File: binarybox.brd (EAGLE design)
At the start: 148.6 x 81.6 mm, 39 parts, among them IC2 MAX7219CNG

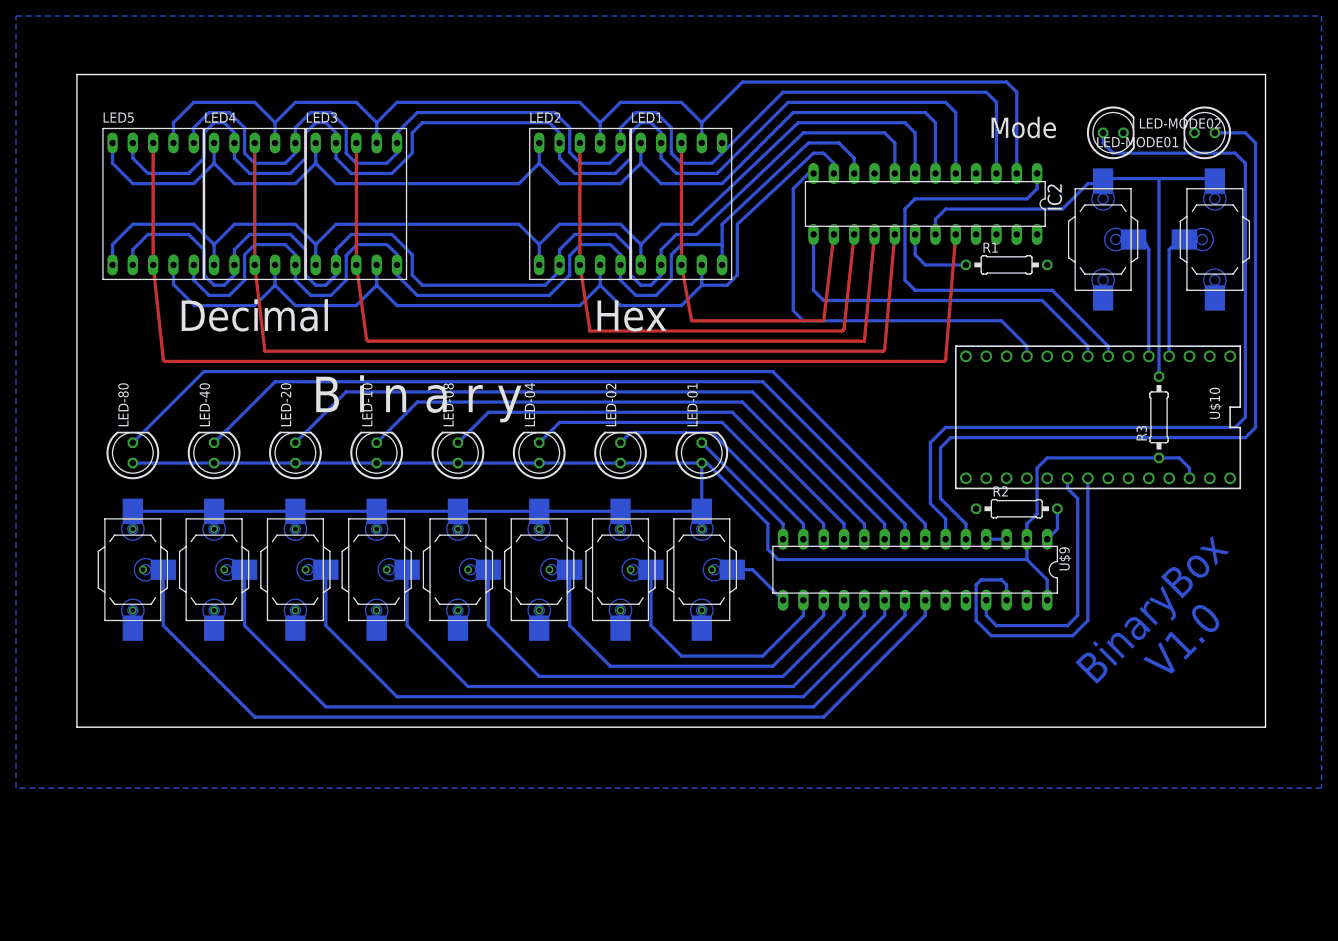
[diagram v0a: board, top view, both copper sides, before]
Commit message: rework - removing io expander
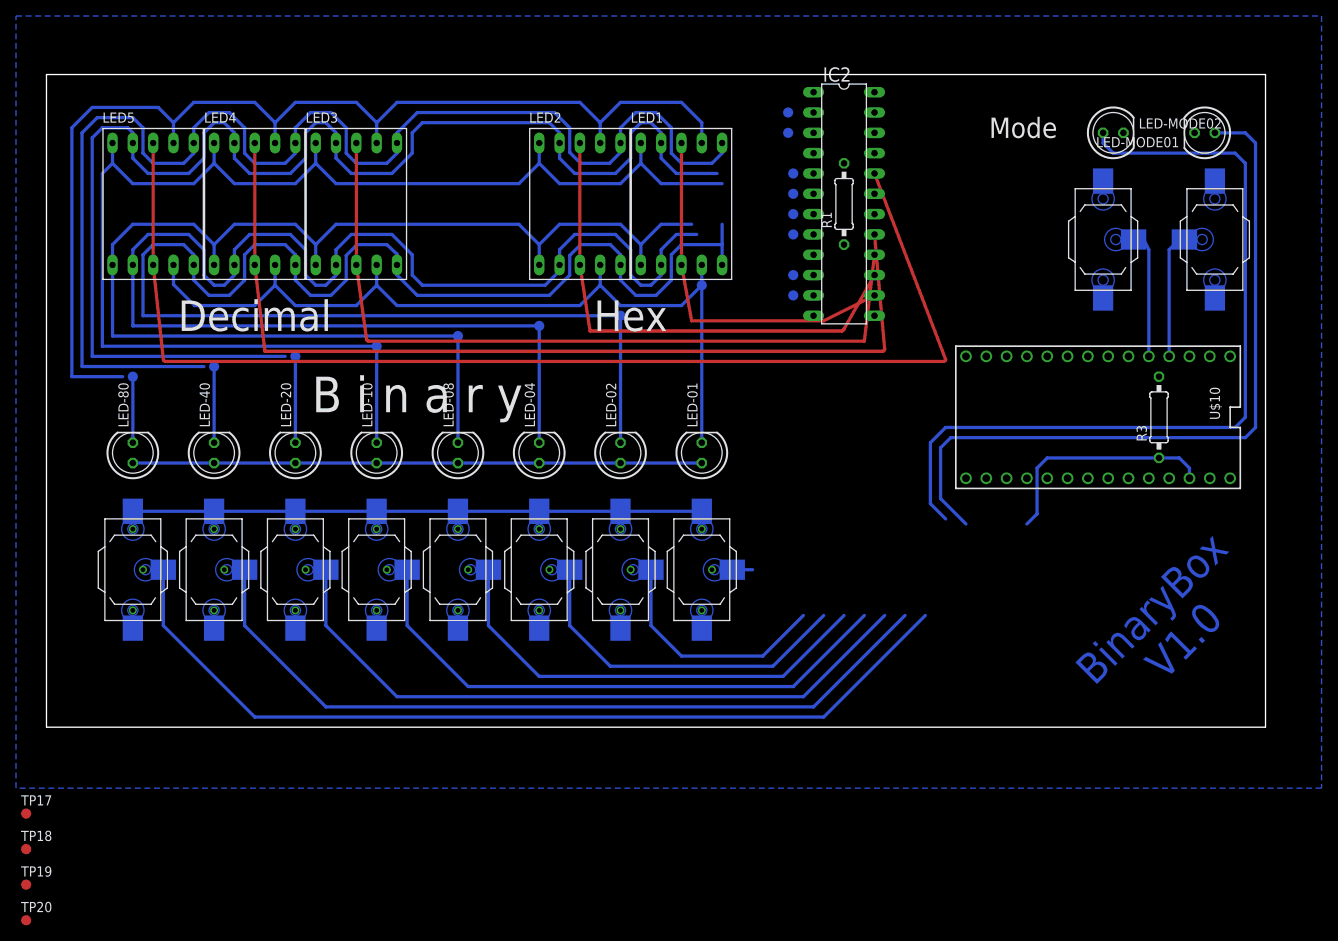
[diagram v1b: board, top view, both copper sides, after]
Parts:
- removed R2: (no value), resistor:0207/10
- removed U$9: MAX6956DIL28-3, max6956-special:DIL28
- added TP10, TP11, TP12, TP13, TP14, TP15, TP16, TP17, TP18, TP19, TP20, TP9: TPB1,27, testpad:B1,27
- moved TP1 29.6 mm to (90.8, 78.1)
- moved TP8 26.5 mm to (90.8, 75.6)
- moved R1 21.7 mm to (97.8, 66.7), turned to 90 degrees
- moved TP5 20.3 mm to (91.4, 70.5)
- moved TP6 18.0 mm to (91.4, 67.9)
- moved TP4 16.1 mm to (91.4, 65.4)
- moved TP2 16.1 mm to (91.4, 55.2)
- moved TP7 14.8 mm to (91.4, 57.8)
- moved TP3 14.8 mm to (91.4, 62.9)
- moved IC2 10.2 mm to (97.8, 66.7), turned to 270 degrees
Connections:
- removed net ISET-IOEXP: R2.2, U$9.1
- removed net SCK: U$10.14/A0
- removed net SCL: U$10.19/A5, U$9.26
- removed net SDA: U$10.18/A4, U$9.25
- new net N$10: TP18.TP, U$10.15/A1
- new net N$11: TP19.TP, U$10.16/A2
- new net N$12: TP20.TP, U$10.17/A3
- new net N$13: U$10.18/A4
- new net N$14: U$10.19/A5
- new net N$15: U$10.20/A6
- new net N$16: U$10.21/A7
- new net N$36: U$10.22/A8
- new net N$37: U$10.23/A9
- new net N$9: TP17.TP, U$10.14/A0
- net GND: no longer R1.2, R2.1, U$9.24, U$9.27, U$9.3, U$9.4
- net INP01: no longer U$9.15
- net INP02: no longer U$9.16
- net INP04: no longer U$9.17
- net INP08: no longer U$9.18
- net INP10: no longer U$9.19
- net INP20: no longer U$9.20
- net INP40: no longer U$9.21
- net INP80: no longer U$9.22
- net LEDMODE01: no longer U$9.6
- net LEDMODE02: no longer U$9.5
- net LEDW01: now also TP16.TP; no longer U$9.14
- net LEDW02: now also TP15.TP; no longer U$9.13
- net LEDW04: now also TP14.TP; no longer U$9.12
- net LEDW08: now also TP13.TP; no longer U$9.11
- net LEDW10: now also TP12.TP; no longer U$9.10
- net LEDW20: now also TP11.TP; no longer U$9.9
- net LEDW40: now also TP10.TP; no longer U$9.8
- net LEDW80: now also TP9.TP; no longer U$9.7
- net SEGE: now also LED-01.A, LED-02.A, LED-04.A, LED-08.A, LED-10.A, LED-20.A, LED-40.A, LED-80.A
- net VCC: now also R1.2; no longer LED-01.A, LED-02.A, LED-04.A, LED-08.A, LED-10.A, LED-20.A, LED-40.A, LED-80.A, U$9.2, U$9.28
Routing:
- net VCC: track 300.3 -> 100.0 mm
- net LEDW80: track 112.5 -> 8.26 mm
- net LEDW40: track 98.8 -> 9.52 mm
- net LEDW20: track 85.0 -> 10.8 mm
- net DIN: track 58.4 -> 0.00 mm
- net N$7: track 0.00 -> 57.8 mm
- net SEGDP: track 127.6 -> 180.4 mm
- net N$6: track 0.00 -> 51.4 mm
- net LOAD: track 50.9 -> 0.00 mm
- net CLK: track 45.4 -> 0.00 mm
- net LEDW08: track 57.5 -> 13.3 mm
- net SCL: track 44.0 -> 0.00 mm
- net SEGD: track 142.6 -> 108.4 mm
- net SEGE: track 133.2 -> 165.7 mm
- net SDA: track 32.1 -> 0.00 mm
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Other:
- board size 148.6 x 81.6 mm -> 152.4 x 81.6 mm
